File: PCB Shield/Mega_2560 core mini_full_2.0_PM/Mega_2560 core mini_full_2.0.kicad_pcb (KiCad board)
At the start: 2 copper layers, 89.5 x 59.7 mm, 132 parts, among them P1 2560-core, P10 RX1TX1, P11 Trim, P12 Stick_left, P13 Stick_right, P14 Switch, P15 LCD_I2C, P16 LCD, P17 BATT, P18 Ecolage, P19 Module_TX, P2 Clock, P20 TTL/RS232, P21 Sw_power, P22 JQ6500_28P, P23 Rot_1, P24 Rot_2, P25 Keys, P26 LCD_Alim, P27 HP, P28 5v/3,3v manches, P3 Option, P30 MiniDCDC3A, P31 Pot2, P32 Pot1, P4 Pot3, P5 Vibreur, P6 Micro_sd, P7 SPIX, P8 Audio, P9 SPI, U1 74LVC1G3157GV, U2 TLP290, U3 TLP290, U4 L4941, U5 LD1117S33TR, U6 MCP604-I/SL, U7 FM24W256, U8 DS3231SN

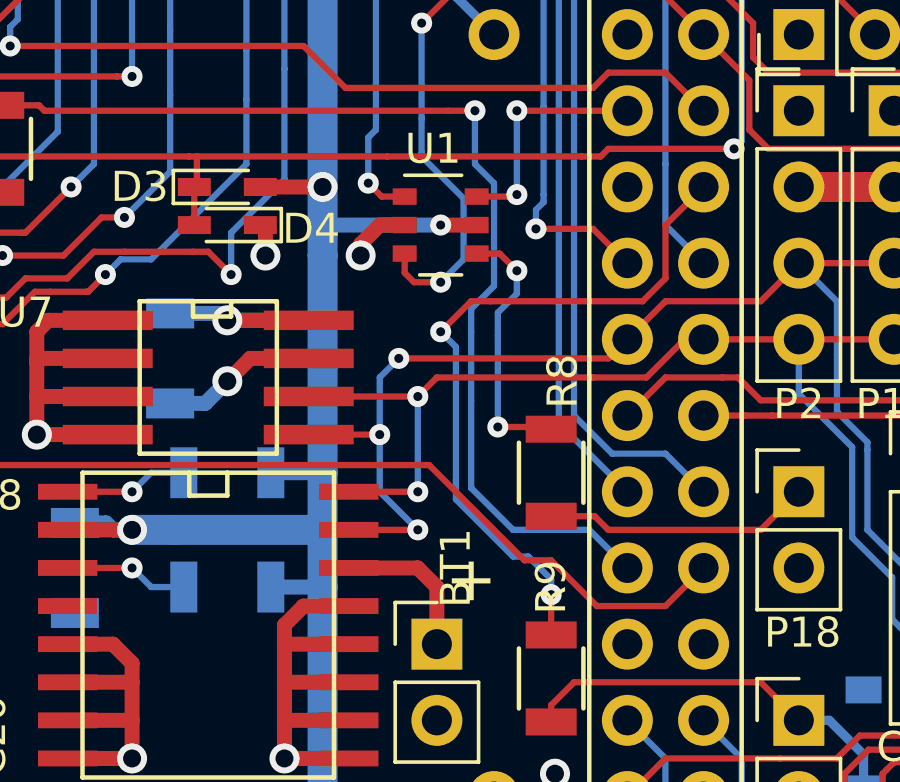
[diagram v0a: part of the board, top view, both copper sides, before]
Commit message: Update pcb shield (add 2 resistors on I2C bus)
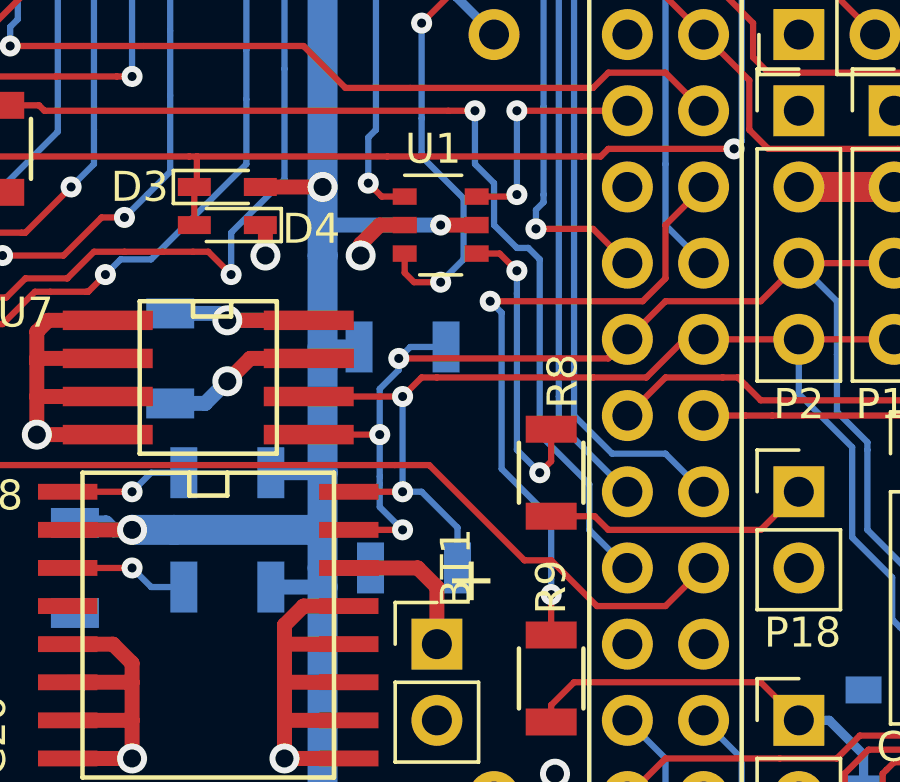
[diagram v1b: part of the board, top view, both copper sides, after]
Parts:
- added R21: 4,7K, anthoperso:R_1206, B.Cu at (192.4, 99.0)
- added R38: 4,7K, anthoperso:R_1206, B.Cu at (192.8, 106.3)
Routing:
- net Scl: track 44.9 -> 48.1 mm
- net VCC: track 423.6 -> 426.4 mm
- net Vibreur: track 23.7 -> 21.7 mm
- net JQ6500Data: track 35.4 -> 33.5 mm
- net Net-(R8-Pad2): track 8.86 -> 10.3 mm
- net Sda: track 48.4 -> 49.4 mm

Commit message: Some changes on schematic's shield (JQ and haptic labels)
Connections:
- net /OpenAVRc_Audio_Haptic/audio_right_in renamed /OpenAVRc_Audio_Haptic/JQ_Left_Out
- net audio_left_in renamed Audio_Buzzer_out

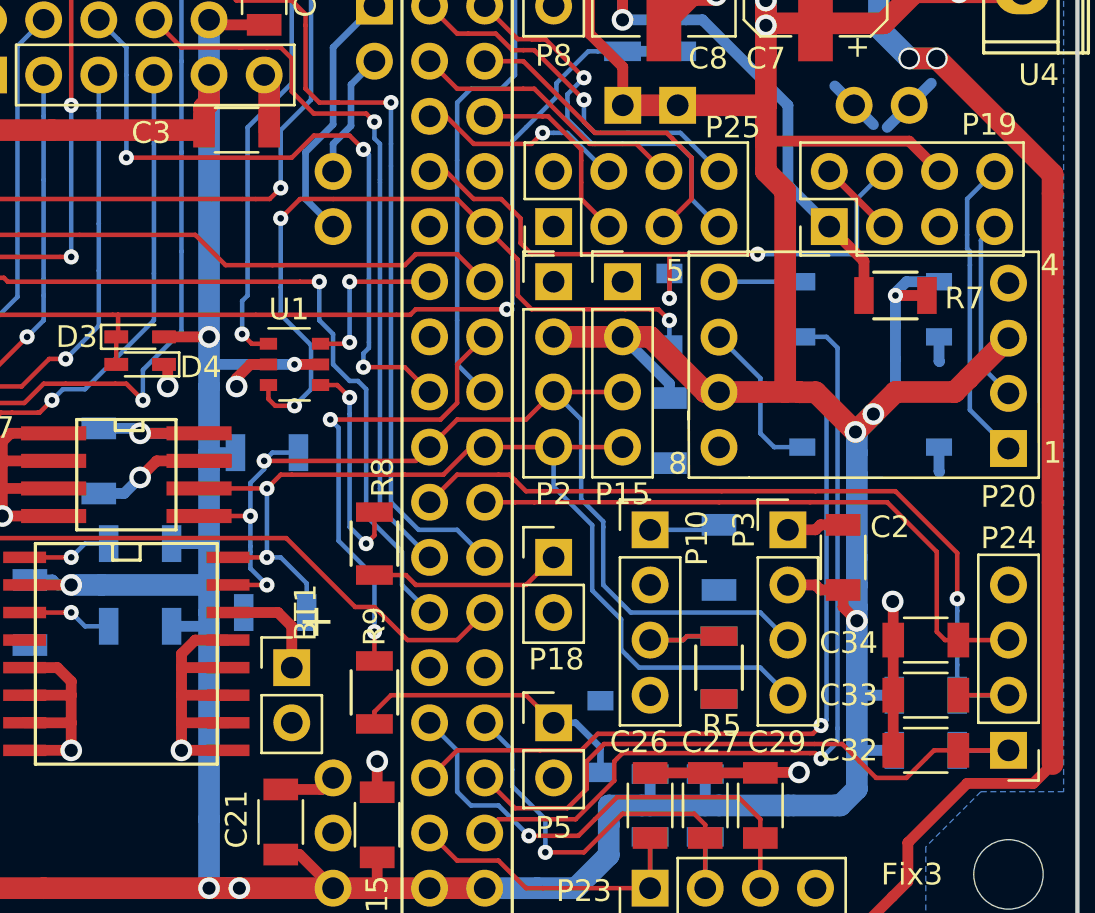
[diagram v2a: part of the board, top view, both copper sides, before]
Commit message: Update schematic sheets
Move Rot_2A on E7 and Rot2A on E6
Add BT_txd1 on D3 and BT_rxd1 on D2
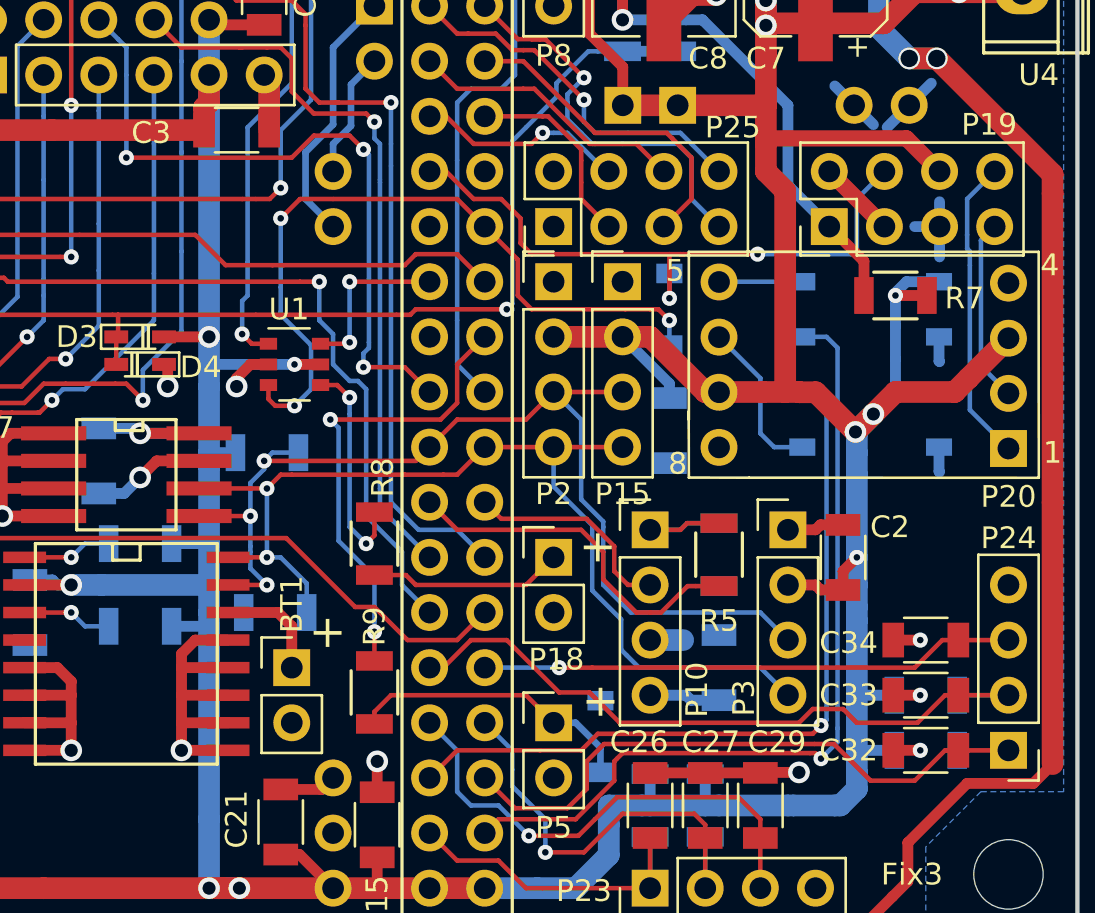
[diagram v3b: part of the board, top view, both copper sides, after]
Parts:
- moved R5 5.21 mm to (213.2, 103.7)
- moved R6 5.21 mm to (213.2, 103.7)
- moved C24 5.08 mm to (213.2, 108.9), turned to 90 degrees
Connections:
- P1 pad D2: Rot_2A -> BT_Rxd1
- P1 pad D3: Rot_2B -> BT_Txd1
- P1 pad E6: (no net) -> Rot_2B
- P1 pad E7: (no net) -> Rot_2A
- P10 pad 1: Net-(C24-Pad1) -> Net-(P10-Pad1)
- P10 pad 2: (no net) -> BT_Rxd1
- P10 pad 3: Net-(P10-Pad3) -> GND
- P10 pad 4: GND -> Net-(C24-Pad1)
- R5 pad 1: Net-(P10-Pad3) -> Net-(P10-Pad1)
- R5 pad 2: (no net) -> BT_Txd1
- R6 pad 1: Net-(P10-Pad3) -> Net-(P10-Pad1)
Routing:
- net BT_Txd1: track 0.00 -> 17.5 mm
- net BT_Rxd1: track 0.00 -> 9.87 mm
- net Net-(P10-Pad1): track 0.00 -> 6.60 mm
- net Net-(P10-Pad3): track 6.50 -> 0.00 mm
- net Rot_2B: track 37.6 -> 32.2 mm, vias 1 -> 0
- net Rot_2A: track 28.9 -> 24.7 mm, vias 0 -> 1
- net GND: track 141.3 -> 143.4 mm, vias 18 -> 20
- net Rot_2push: track 30.2 -> 30.8 mm

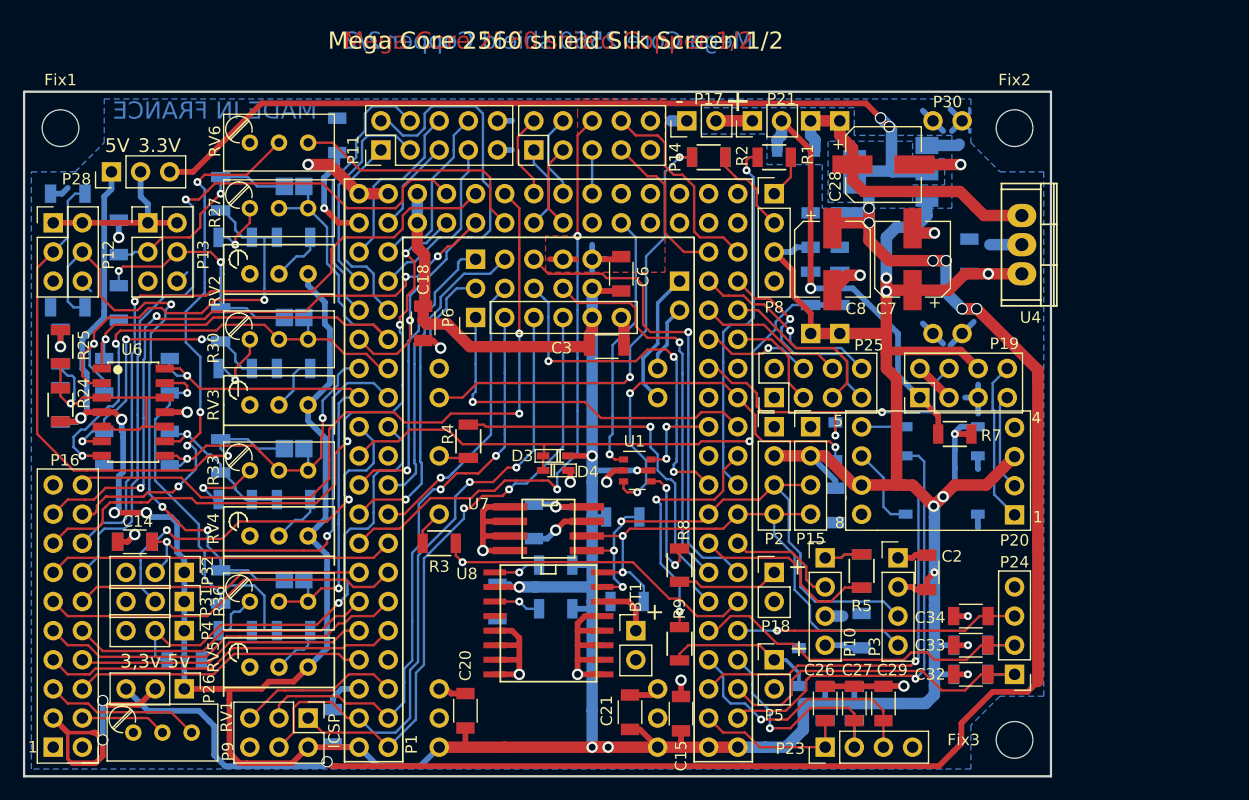
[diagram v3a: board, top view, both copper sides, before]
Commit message: Update schematic and pcb
Add PM-5033 as other dc/dc option
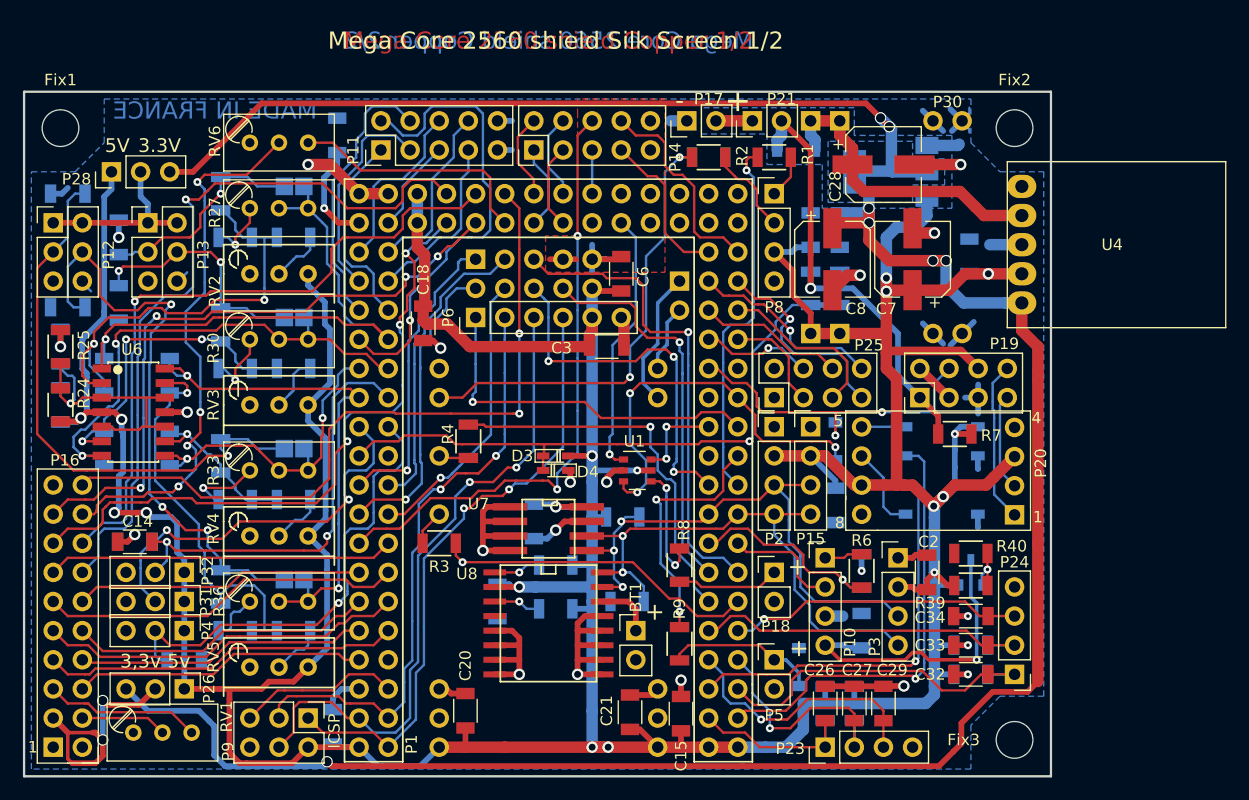
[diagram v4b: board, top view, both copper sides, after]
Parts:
- added Q1: BSS84, MegaCore_Shield:SOT-23_MOS_P, B.Cu at (222.7, 103.8)
- added R39: 47K, Resistors_SMD:R_1206, F.Cu at (222.7, 104.9)
- added R40: 100, Resistors_SMD:R_1206, F.Cu at (222.7, 102.1)
- R5: value 1K -> 4K7; moved to B.Cu
- R6: value 2,2K -> 4K7; moved to F.Cu
- U4: value L4941 -> PM5033; footprint Power_Integrations:TO-220 -> MegaCore_Shield:Pm5033_sil5
- moved U4 5.08 mm to (227.2, 70.1), turned to 0 degrees
- turned R5 to 90 degrees
- turned R6 to 90 degrees
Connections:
- R5 pad 1: Net-(P10-Pad1) -> BT_Txd1
- R5 pad 2: BT_Txd1 -> GND
- R6 pad 1: Net-(P10-Pad1) -> BT_Txd1
- R6 pad 2: GND -> Net-(P10-Pad1)
- U4 pad 1: /OpenAVRc_Power/DCDC_IN+ -> (no net)
- U4 pad 2: GND -> /OpenAVRc_Power/DCDC_IN+
- U4 pad 3: VCC -> GND
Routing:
- net Net-(C24-Pad1): track 3.27 -> 42.2 mm, vias 0 -> 1
- net VCC: track 426.6 -> 431.2 mm
- net Net-(Q1-PadG): track 0.00 -> 4.36 mm, vias 0 -> 1
- net Net-(P10-Pad1): track 6.60 -> 3.30 mm
- net Rot_2B: track 32.2 -> 30.6 mm
- net GND: track 143.4 -> 144.9 mm, vias 20 -> 21
- net Rot_2A: track 24.7 -> 25.7 mm
- net BT_Txd1: track 17.5 -> 18.5 mm, vias 0 -> 1
- net +3.3V: track 230.1 -> 231.1 mm, vias 9 -> 7
- net /OpenAVRc_CoreConnects/Lcd_cs: track 65.1 -> 64.4 mm

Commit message: Update shield files on good place
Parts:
- R18, R19, R22, R23: value 5.1k -> 5.1K
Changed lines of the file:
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@@
       (effects (font (size 1 1) (thickness 0.15)) (justify mirror))
     )
-    (fp_text value 5.1k (at 0.127 -0.127 270) (layer B.Fab)
+    (fp_text value 5.1K (at 0.127 -0.127 270) (layer B.Fab)
       (effects (font (size 1 1) (thickness 0.15)) (justify mirror))
     )
@@
       (effects (font (size 1 1) (thickness 0.15)) (justify mirror))
     )
-    (fp_text value 5.1k (at 0 0) (layer B.Fab)
+    (fp_text value 5.1K (at 0 0) (layer B.Fab)
       (effects (font (size 1 1) (thickness 0.15)) (justify mirror))
     )
@@
       (effects (font (size 1 1) (thickness 0.15)) (justify mirror))
     )
-    (fp_text value 5.1k (at 0 -0.127 270) (layer B.Fab)
+    (fp_text value 5.1K (at 0 -0.127 270) (layer B.Fab)
       (effects (font (size 1 1) (thickness 0.15)) (justify mirror))
     )
@@
       (effects (font (size 1 1) (thickness 0.15)) (justify mirror))
     )
-    (fp_text value 5.1k (at 0 0) (layer B.Fab)
-      (effects (font (size 1 1) (thickness 0.15)) (justify mirror))
-    )
+    (fp_text value 5.1K (at 0 0) (layer B.Fab)
+      (effects (font (size 1 1) (thickness 0.15)) (justify mirror))
+    )

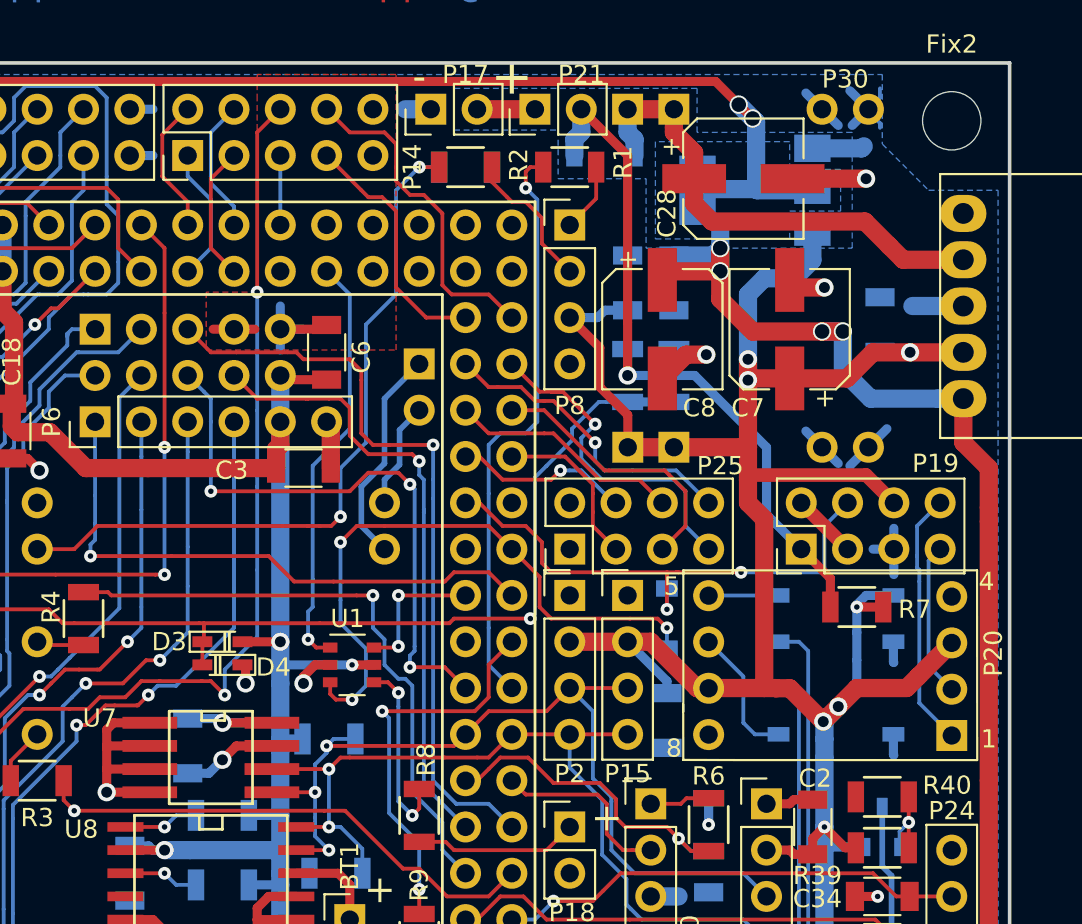
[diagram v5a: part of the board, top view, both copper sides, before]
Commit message: Add Hold Power feature
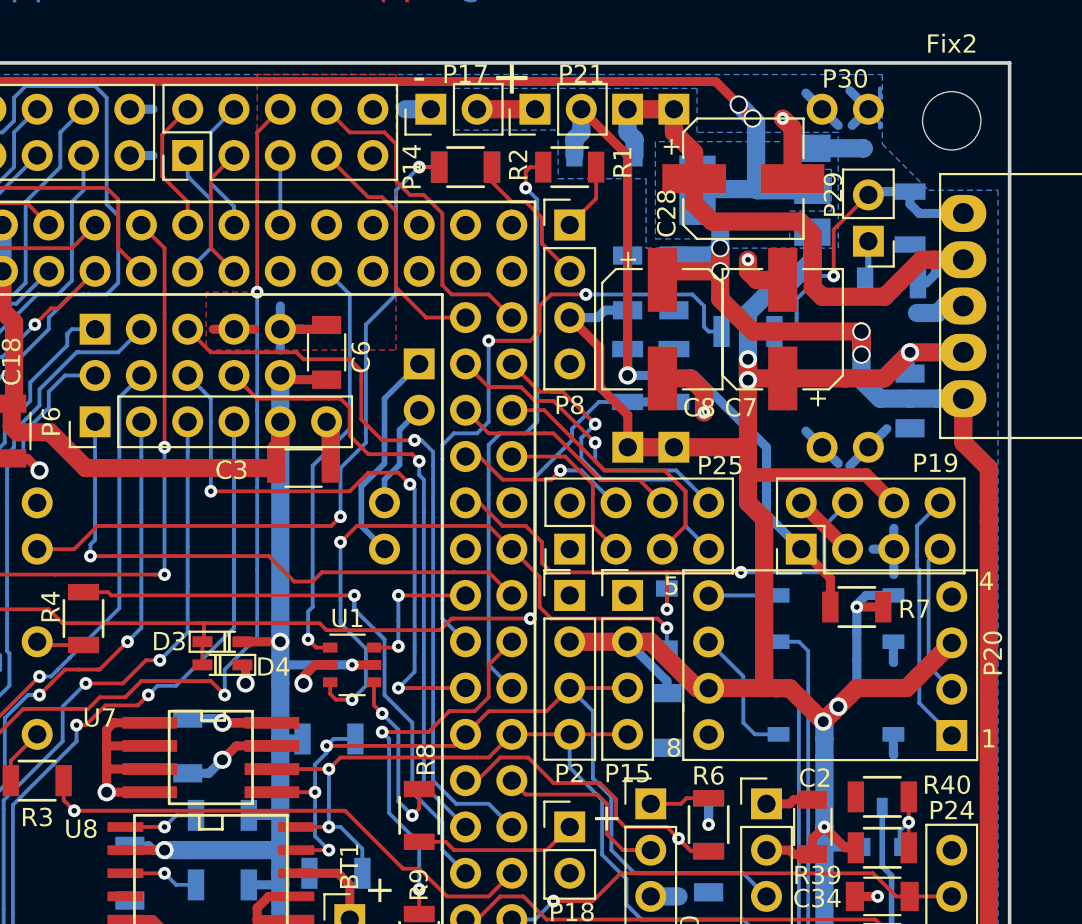
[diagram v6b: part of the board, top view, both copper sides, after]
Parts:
- added P29: Sw_On, Pin_Headers:Pin_Header_Straight_1x02_Pitch2.54mm, F.Cu at (222.0, 71.7)
- added R41: 33K, Resistors_SMD:R_1206, B.Cu at (223.2, 73.9)
- added R42: 2.2K, Resistors_SMD:R_1206, B.Cu at (215.4, 76.6)
- added R43: 10K, Resistors_SMD:R_1206, B.Cu at (224.3, 70.4)
- moved C31 4.50 mm to (224.3, 80.4), turned to 270 degrees
- moved C7 0.38 mm to (217.3, 76.5)
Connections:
- P1 pad H4: (no net) -> Hold_Power
- U4 pad 1: (no net) -> Net-(P29-Pad2)
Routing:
- net Hold_Power: track 0.00 -> 35.0 mm, vias 0 -> 2
- net Net-(P29-Pad2): track 0.00 -> 16.7 mm, vias 0 -> 1
- net /OpenAVRc_Power/DCDC_IN+: track 26.9 -> 33.6 mm
- net Net-(P29-Pad1): track 0.00 -> 4.47 mm
- net Xmitter_SCK: track 32.2 -> 33.8 mm
- net VCC: track 431.2 -> 430.1 mm
- net JQ6500Data: track 33.5 -> 34.4 mm
- net GND: track 144.9 -> 145.7 mm
- net Xmitter_MISO: track 41.9 -> 41.2 mm
- net Vibreur: track 21.7 -> 21.0 mm
